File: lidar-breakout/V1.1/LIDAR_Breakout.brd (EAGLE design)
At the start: 36.5 x 88 mm, 89 parts, among them J1 UX60-MB-5S8, P1 MOLEX 0436500200, X1 TSX-3225 16.0000MF18X-AC0

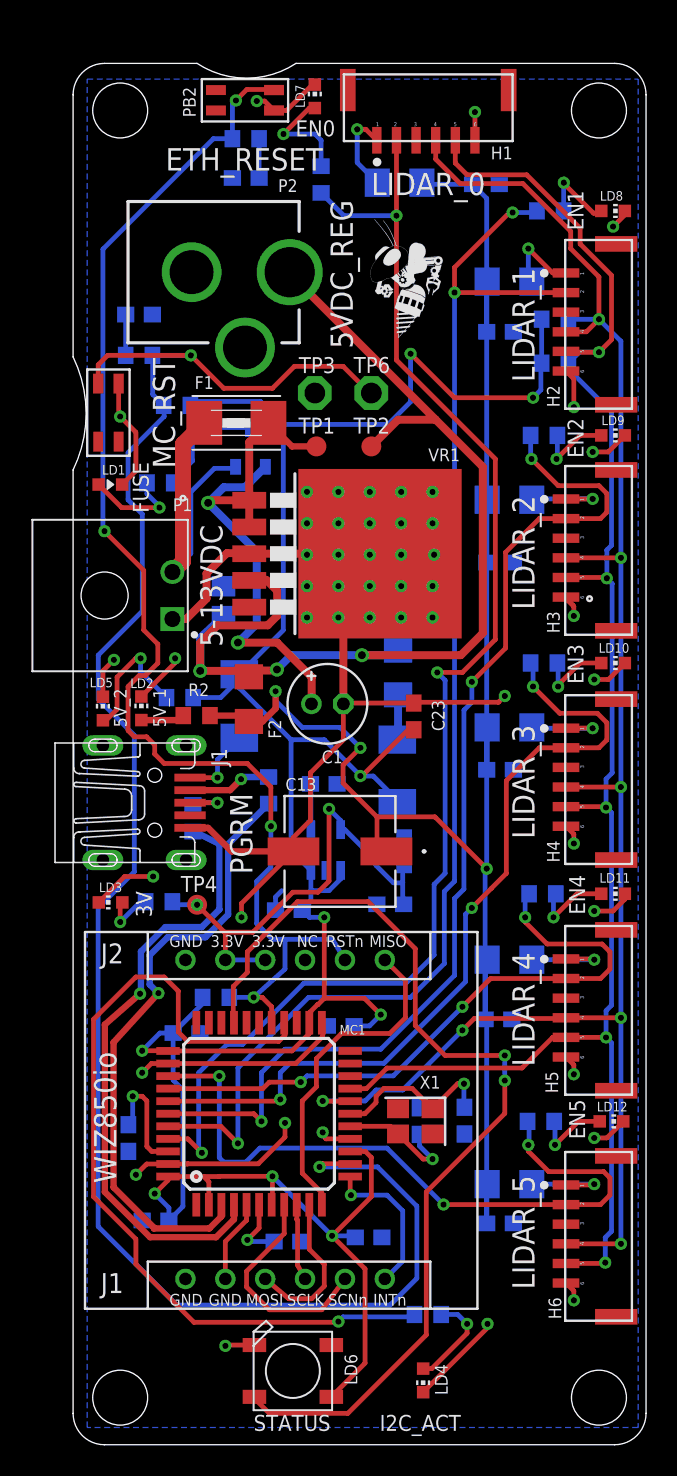
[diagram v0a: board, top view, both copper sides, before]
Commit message: Added POGO Pads
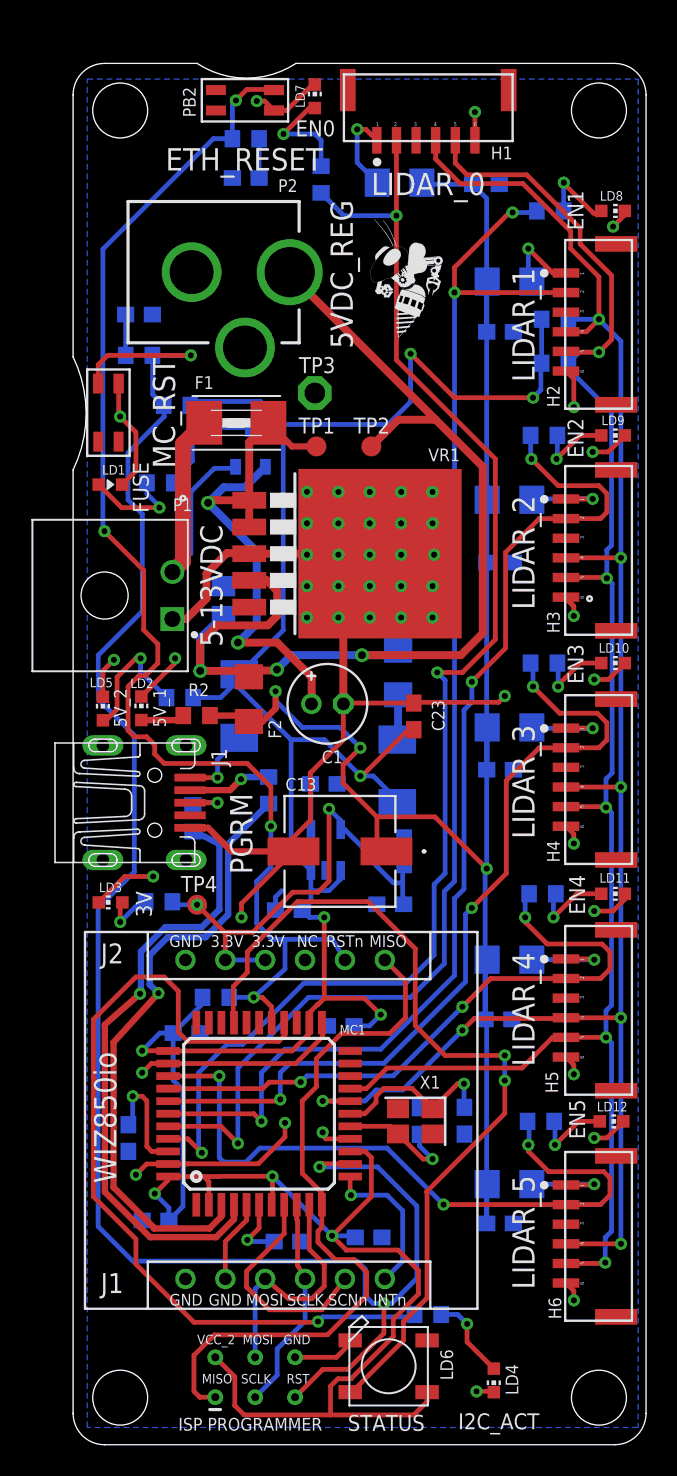
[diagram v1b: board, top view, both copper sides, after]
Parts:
- removed TP6: PTR1PAD1-13, testpad:P1-13
- added J2: AVR_SPI_PROG_3X2TESTPOINTS, SparkFun-Connectors:2X3_TEST_POINTS
- moved LD6 6.11 mm to (20.1, 5.00)
- moved LD4 4.50 mm to (26.8, 4.10)
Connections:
- net GND: now also J2.6
- net MISO_ETH: now also J2.1
- net MOSI_ETH: now also J2.4
- net RST_MC: now also J2.5; no longer TP6.TP
- net SCLK_ETH: now also J2.3
- net VCC_2: now also J2.2
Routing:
- net MISO_ETH: track 21.2 -> 45.4 mm
- net VCC_2: track 171.5 -> 194.9 mm
- net SCLK_ETH: track 4.86 -> 13.7 mm
- net STATUS_PWM: track 63.0 -> 55.2 mm
- net MOSI_ETH: track 10.1 -> 15.4 mm
- net RST_MC: track 120.6 -> 117.1 mm, vias 2 -> 3
- net GND: track 141.2 -> 138.4 mm, vias 49 -> 48
- net N$2: track 6.23 -> 5.45 mm
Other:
- board text added: "GND"
- board text added: "ISP PROGRAMMER"
- board text added: "MISO"
- board text added: "MOSI"
- board text added: "RST"
- board text added: "SCLK"
- board text added: "VCC_2"

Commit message: Updated Reset PB
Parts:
- PB1: device RoboJackets-Switches:RESET_PB_RA -> RoboJackets-Switches:TACT_PB_RA
- moved C26 10.9 mm to (15.1, 71.0)
- moved R19 6.24 mm to (10.3, 68.1), turned to 180 degrees
- moved P2 4.20 mm to (0.10, 78.9)
- moved PB1 4.20 mm to (0.00, 72.6)
- moved R7 3.00 mm to (15.8, 83.6)
- moved TP1 2.50 mm to (18.0, 63.6)
- moved H1 2.39 mm to (29.3, 89.3)
- moved C25 2.00 mm to (11.0, 82.7)
- moved LD7 2.00 mm to (15.4, 87.9)
- moved PB2 2.00 mm to (13.7, 89.0)
- moved R18 2.00 mm to (11.0, 85.2)
- moved TP2 2.00 mm to (21.0, 63.6)
- moved F1 1.92 mm to (12.3, 64.8)
- moved TP3 1.84 mm to (16.7, 68.3)
- moved R1 0.95 mm to (6.92, 67.1), turned to 90 degrees
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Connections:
- net GND: now also PB1.P$2; no longer PB1.P$3
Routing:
- net LDR0_EN: track 88.7 -> 93.7 mm
- net RST_MC: track 117.1 -> 112.7 mm, vias 3 -> 2
- net GND: track 138.4 -> 134.7 mm
- net RST_ETH: track 84.9 -> 88.3 mm
- net LDR0_LED: track 6.90 -> 4.20 mm
- net 5VREG: track 69.9 -> 72.2 mm
- net N$11: track 2.60 -> 4.30 mm
- net VCC_2: track 194.9 -> 193.5 mm
- net VIN: track 36.1 -> 37.1 mm
- net SCL: track 115.4 -> 114.5 mm
- net SDA: track 109.9 -> 109.1 mm
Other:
- board size 36.5 x 88 mm -> 36.5 x 90 mm

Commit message: Minor fixes/optimization
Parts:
- moved F1 1.40 mm to (13.7, 64.8)
- moved TP1 1.10 mm to (19.1, 63.6)
- moved TP2 1.10 mm to (22.1, 63.6)
- moved TP3 1.00 mm to (15.7, 68.3)
- moved P2 0.30 mm to (0.10, 78.6)
- moved R1 0.10 mm to (6.92, 67.2)
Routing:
- net GND: track 134.7 -> 145.7 mm
- net VIN: track 37.1 -> 36.0 mm
- net 5VREG: track 72.2 -> 71.2 mm
- net RST_MC: track 112.7 -> 113.4 mm

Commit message: Updated LED resistor values
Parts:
- R10, R11, R12, R7, R8, R9: value 1 kΩ -> 200Ω
- R13, R14, R17, R2, R3: value 1 kΩ -> 300Ω
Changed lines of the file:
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@@
 <attribute name="VALUE" x="10.547" y="41.055" size="1.27" layer="28" rot="MR90"/>
 </element>
-<element name="R14" library="rcl" library_urn="urn:adsk.eagle:library:334" package="R0603" package3d_urn="urn:adsk.eagle:package:23555/2" value="1 kΩ" x="5.558" y="61.277" smashed="yes" rot="MR0">
+<element name="R14" library="rcl" library_urn="urn:adsk.eagle:library:334" package="R0603" package3d_urn="urn:adsk.eagle:package:23555/2" value="300Ω" x="5.558" y="61.277" smashed="yes" rot="MR0">
 <attribute name="NAME" x="3.388" y="62.293" size="0.8128" layer="26" font="vector" rot="MR270"/>
 <attribute name="SPICEPREFIX" value="R" x="-32.542" y="-16.193" size="1.778" layer="28" rot="MR0" display="off"/>
 <attribute name="VALUE" x="6.193" y="59.372" size="1.27" layer="28" rot="MR0"/>
 </element>
-<element name="R2" library="rcl" library_urn="urn:adsk.eagle:library:334" package="R0603" package3d_urn="urn:adsk.eagle:package:23555/2" value="1 kΩ" x="7.869" y="46.45" smashed="yes">
+<element name="R2" library="rcl" library_urn="urn:adsk.eagle:library:334" package="R0603" package3d_urn="urn:adsk.eagle:package:23555/2" value="300Ω" x="7.869" y="46.45" smashed="yes">
 <attribute name="NAME" x="7.334" y="47.685" size="0.8128" layer="25" font="vector"/>
 <attribute name="SPICEPREFIX" value="R" x="37.079" y="-31.02" size="1.778" layer="27" display="off"/>
 <attribute name="VALUE" x="7.234" y="44.545" size="1.27" layer="27"/>
 </element>
-<element name="R13" library="rcl" library_urn="urn:adsk.eagle:library:334" package="R0603" package3d_urn="urn:adsk.eagle:package:23555/2" value="1 kΩ" x="5.472121875" y="34.5944" smashed="yes" rot="MR180">
+<element name="R13" library="rcl" library_urn="urn:adsk.eagle:library:334" package="R0603" package3d_urn="urn:adsk.eagle:package:23555/2" value="300Ω" x="5.472121875" y="34.5944" smashed="yes" rot="MR180">
 <attribute name="NAME" x="3.462878125" y="34.1406" size="0.8128" layer="26" font="vector" rot="MR0"/>
 <attribute name="SPICEPREFIX" value="R" x="61.352121875" y="112.0644" size="1.778" layer="28" rot="MR180" display="off"/>
@@
 <attribute name="NAME" x="7" y="88.5" size="0.8128" layer="21" font="vector" rot="R270"/>
 </element>
-<element name="R7" library="rcl" library_urn="urn:adsk.eagle:library:334" package="R0603" package3d_urn="urn:adsk.eagle:package:23555/2" value="1 kΩ" x="15.8" y="83.6" smashed="yes" rot="MR90">
+<element name="R7" library="rcl" library_urn="urn:adsk.eagle:library:334" package="R0603" package3d_urn="urn:adsk.eagle:package:23555/2" value="200Ω" x="15.8" y="83.6" smashed="yes" rot="MR90">
 <attribute name="NAME" x="16.435" y="80.935" size="0.8128" layer="26" font="vector" rot="MR0"/>
 <attribute name="SPICEPREFIX" value="R" x="15.8" y="83.6" size="1.778" layer="28" rot="MR90" display="off"/>
@@
 <attribute name="VALUE" x="17.305" y="87.265" size="1.27" layer="27" rot="R90"/>
 </element>
-<element name="R8" library="rcl" library_urn="urn:adsk.eagle:library:334" package="R0603" package3d_urn="urn:adsk.eagle:package:23555/2" value="1 kΩ" x="30.4" y="78.6" smashed="yes" rot="MR180">
+<element name="R8" library="rcl" library_urn="urn:adsk.eagle:library:334" package="R0603" package3d_urn="urn:adsk.eagle:package:23555/2" value="200Ω" x="30.4" y="78.6" smashed="yes" rot="MR180">
 <attribute name="NAME" x="29.765" y="77.365" size="0.8128" layer="26" font="vector" rot="MR180"/>
 <attribute name="SPICEPREFIX" value="R" x="30.4" y="78.6" size="1.778" layer="28" rot="MR180" display="off"/>
@@
 <attribute name="VALUE" x="33.765" y="76.695" size="1.27" layer="27"/>
 </element>
-<element name="R9" library="rcl" library_urn="urn:adsk.eagle:library:334" package="R0603" package3d_urn="urn:adsk.eagle:package:23555/2" value="1 kΩ" x="30" y="64.3" smashed="yes" rot="MR180">
+<element name="R9" library="rcl" library_urn="urn:adsk.eagle:library:334" package="R0603" package3d_urn="urn:adsk.eagle:package:23555/2" value="200Ω" x="30" y="64.3" smashed="yes" rot="MR180">
 <attribute name="NAME" x="27.335" y="63.765" size="0.8128" layer="26" font="vector" rot="MR90"/>
 <attribute name="SPICEPREFIX" value="R" x="30" y="64.3" size="1.778" layer="28" rot="MR180" display="off"/>
 <attribute name="VALUE" x="29.365" y="66.205" size="1.27" layer="28" rot="MR180"/>
 </element>
-<element name="R10" library="rcl" library_urn="urn:adsk.eagle:library:334" package="R0603" package3d_urn="urn:adsk.eagle:package:23555/2" value="1 kΩ" x="30" y="49.8" smashed="yes" rot="MR180">
+<element name="R10" library="rcl" library_urn="urn:adsk.eagle:library:334" package="R0603" package3d_urn="urn:adsk.eagle:package:23555/2" value="200Ω" x="30" y="49.8" smashed="yes" rot="MR180">
 <attribute name="NAME" x="29.065" y="51.765" size="0.8128" layer="26" font="vector" rot="MR180"/>
 <attribute name="SPICEPREFIX" value="R" x="30" y="49.8" size="1.778" layer="28" rot="MR180" display="off"/>
 <attribute name="VALUE" x="29.365" y="51.705" size="1.27" layer="28" rot="MR180"/>
 </element>
-<element name="R11" library="rcl" library_urn="urn:adsk.eagle:library:334" package="R0603" package3d_urn="urn:adsk.eagle:package:23555/2" value="1 kΩ" x="29.9" y="35.1" smashed="yes" rot="MR180">
+<element name="R11" library="rcl" library_urn="urn:adsk.eagle:library:334" package="R0603" package3d_urn="urn:adsk.eagle:package:23555/2" value="200Ω" x="29.9" y="35.1" smashed="yes" rot="MR180">
 <attribute name="NAME" x="31.935" y="34.165" size="0.8128" layer="26" font="vector" rot="SMR90"/>
 <attribute name="SPICEPREFIX" value="R" x="29.9" y="35.1" size="1.778" layer="28" rot="MR180" display="off"/>
 <attribute name="VALUE" x="29.265" y="37.005" size="1.27" layer="28" rot="MR180"/>
 </element>
-<element name="R12" library="rcl" library_urn="urn:adsk.eagle:library:334" package="R0603" package3d_urn="urn:adsk.eagle:package:23555/2" value="1 kΩ" x="29.8" y="20.6" smashed="yes" rot="MR180">
+<element name="R12" library="rcl" library_urn="urn:adsk.eagle:library:334" package="R0603" package3d_urn="urn:adsk.eagle:package:23555/2" value="200Ω" x="29.8" y="20.6" smashed="yes" rot="MR180">
 <attribute name="NAME" x="30.735" y="21.935" size="0.8128" layer="26" font="vector" rot="MR0"/>
 <attribute name="SPICEPREFIX" value="R" x="29.8" y="20.6" size="1.778" layer="28" rot="MR180" display="off"/>
@@
 <attribute name="VALUE" x="24.895" y="4.735" size="1.27" layer="27" rot="R270"/>
 </element>
-<element name="R3" library="rcl" library_urn="urn:adsk.eagle:library:334" package="R0603" package3d_urn="urn:adsk.eagle:package:23555/2" value="1 kΩ" x="22.6" y="8.3" smashed="yes" rot="MR0">
+<element name="R3" library="rcl" library_urn="urn:adsk.eagle:library:334" package="R0603" package3d_urn="urn:adsk.eagle:package:23555/2" value="300Ω" x="22.6" y="8.3" smashed="yes" rot="MR0">
 <attribute name="NAME" x="21.965" y="10.365" size="0.8128" layer="26" font="vector" rot="MR180"/>
 <attribute name="SPICEPREFIX" value="R" x="22.6" y="8.3" size="1.778" layer="28" rot="MR0" display="off"/>
@@
 <attribute name="VALUE" x="23.113" y="50.597" size="1.27" layer="28" rot="MR270"/>
 </element>
-<element name="R17" library="rcl" library_urn="urn:adsk.eagle:library:334" package="R0603" package3d_urn="urn:adsk.eagle:package:23555/2" value="1 kΩ" x="6.8" y="47.6" smashed="yes" rot="MR180">
+<element name="R17" library="rcl" library_urn="urn:adsk.eagle:library:334" package="R0603" package3d_urn="urn:adsk.eagle:package:23555/2" value="300Ω" x="6.8" y="47.6" smashed="yes" rot="MR180">
 <attribute name="NAME" x="4.035" y="46.665" size="0.8128" layer="26" rot="MR90"/>
 <attribute name="SPICEPREFIX" value="R" x="6.8" y="47.6" size="1.778" layer="28" rot="MR180" display="off"/>

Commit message: Minor Changes, DRC, Design Review Prep
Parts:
- moved TP3 0.50 mm to (15.7, 68.8)
- moved C26 0.40 mm to (15.1, 71.4)
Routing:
- net GND: track 145.7 -> 156.7 mm, vias 48 -> 44
- net RST_MC: track 113.4 -> 114.7 mm
- net VCC_2: track 193.6 -> 194.4 mm
- net RST_ETH: track 88.3 -> 87.5 mm

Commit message: DR Ready
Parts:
- moved C11 0.70 mm to (27.2, 70.2)
- moved C21 0.58 mm to (20.8, 37.3)
- moved C6 0.50 mm to (20.2, 33.9)
- moved R5 0.20 mm to (30.9, 68.9)
- moved R6 0.20 mm to (30.9, 71.7)
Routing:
- net VCC_1: track 119.5 -> 120.2 mm

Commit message: Design Review Updates
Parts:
- C25: value 1 uF -> 0.1uF
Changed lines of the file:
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@@
 <?xml version="1.0" encoding="utf-8"?>
 <!DOCTYPE eagle SYSTEM "eagle.dtd">
-<eagle version="9.3.0">
+<eagle version="9.2.2">
 <drawing>
 <settings>
-<setting alwaysvectorfont="yes"/>
+<setting alwaysvectorfont="no"/>
 <setting verticaltext="up"/>
 </settings>
 <grid distance="0.1" unitdist="mm" unit="mm" style="lines" multiple="1" display="yes" altdistance="0.05" altunitdist="mm" altunit="mm"/>
 <layers>
-<layer number="1" name="Top" color="4" fill="1" visible="yes" active="yes"/>
+<layer number="1" name="Top" color="4" fill="1" visible="no" active="yes"/>
 <layer number="2" name="Route2" color="16" fill="1" visible="no" active="no"/>
 <layer number="3" name="Route3" color="17" fill="1" visible="no" active="no"/>
@@
 <layer number="19" name="Unrouted" color="6" fill="1" visible="yes" active="yes"/>
 <layer number="20" name="Dimension" color="24" fill="1" visible="yes" active="yes"/>
-<layer number="21" name="tPlace" color="7" fill="1" visible="yes" active="yes"/>
+<layer number="21" name="tPlace" color="7" fill="1" visible="no" active="yes"/>
 <layer number="22" name="bPlace" color="7" fill="1" visible="yes" active="yes"/>
-<layer number="23" name="tOrigins" color="15" fill="1" visible="yes" active="yes"/>
+<layer number="23" name="tOrigins" color="15" fill="1" visible="no" active="yes"/>
 <layer number="24" name="bOrigins" color="15" fill="1" visible="yes" active="yes"/>
-<layer number="25" name="tNames" color="7" fill="1" visible="yes" active="yes"/>
+<layer number="25" name="tNames" color="7" fill="1" visible="no" active="yes"/>
 <layer number="26" name="bNames" color="7" fill="1" visible="yes" active="yes"/>
 <layer number="27" name="tValues" color="7" fill="1" visible="no" active="yes"/>
@@
 <layer number="37" name="tTest" color="7" fill="1" visible="no" active="yes"/>
 <layer number="38" name="bTest" color="7" fill="1" visible="no" active="yes"/>
-<layer number="39" name="tKeepout" color="4" fill="11" visible="yes" active="yes"/>
+<layer number="39" name="tKeepout" color="4" fill="11" visible="no" active="yes"/>
 <layer number="40" name="bKeepout" color="1" fill="11" visible="yes" active="yes"/>
-<layer number="41" name="tRestrict" color="4" fill="10" visible="yes" active="yes"/>
+<layer number="41" name="tRestrict" color="4" fill="10" visible="no" active="yes"/>
 <layer number="42" name="bRestrict" color="1" fill="10" visible="yes" active="yes"/>
 <layer number="43" name="vRestrict" color="2" fill="10" visible="no" active="yes"/>
@@
 <layer number="49" name="Reference" color="7" fill="1" visible="no" active="yes"/>
 <layer number="50" name="dxf" color="7" fill="1" visible="no" active="no"/>
-<layer number="51" name="tDocu" color="7" fill="1" visible="yes" active="yes"/>
+<layer number="51" name="tDocu" color="7" fill="1" visible="no" active="yes"/>
 <layer number="52" name="bDocu" color="7" fill="1" visible="yes" active="yes"/>
 <layer number="53" name="tGND_GNDA" color="7" fill="9" visible="no" active="no"/>
@@
 <text x="8.1" y="58.6" size="1.4224" layer="21" font="vector" rot="R270">5-13VDC</text>
 <text x="10" y="41.5" size="1.4224" layer="21" font="vector" rot="R270">PGRM</text>
-<wire x1="14.2" y1="90" x2="7.9" y2="90" width="0.0762" layer="20" curve="-66.549776"/>
+<wire x1="14.2" y1="90" x2="7.9" y2="90" width="0" layer="20" curve="-66.549776"/>
 <wire x1="29.3" y1="72.7" x2="32.5" y2="72.7" width="0.1016" layer="22"/>
 <wire x1="32.5" y1="72.7" x2="32.5" y2="70.7" width="0.1016" layer="22"/>
@@
 <attribute name="PINS" value="5" x="-1.2" y="40.9" size="1.778" layer="27" display="off"/>
 </element>
-<element name="C25" library="resistor" library_urn="urn:adsk.eagle:library:348" package="C0603" package3d_urn="urn:adsk.eagle:package:26138/1" value="1 uF" x="11" y="82.7" smashed="yes" rot="MR0">
+<element name="C25" library="resistor" library_urn="urn:adsk.eagle:library:348" package="C0603" package3d_urn="urn:adsk.eagle:package:26138/1" value="0.1uF" x="11" y="82.7" smashed="yes" rot="MR0">
 <attribute name="NAME" x="8.135" y="81.765" size="0.8128" layer="26" rot="MR90"/>
 <attribute name="VALUE" x="11.635" y="80.795" size="1.27" layer="28" rot="MR0"/>

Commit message: Post Design Review Updates
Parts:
- removed R18, R19: 1 kΩ, rcl:R0603
- D1, D2: value (none) -> APD340VRTR-G1
- R13, R14, R17, R2, R3: value 300Ω -> 330Ω
- moved C26 5.42 mm to (10.8, 68.1)
- moved R3 2.73 mm to (25.0, 9.60)
- moved C25 2.50 mm to (11.0, 85.2), turned to 180 degrees
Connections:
- removed net N$10: C25.1, R18.2
- removed net N$11: C26.1, R19.2
- net RST_ETH: now also C25.1; no longer R18.1
- net RST_MC: now also C26.1; no longer R19.1
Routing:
- net N$11: track 4.58 -> 0.00 mm
- net I2C_ACT: track 53.7 -> 56.7 mm
- net GND: track 156.6 -> 159.4 mm
- net N$10: track 2.50 -> 0.00 mm
- net RST_MC: track 114.7 -> 113.6 mm
- net N$2: track 5.45 -> 6.27 mm
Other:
- board text added: "LIDAR BREAKOUT REV: 1.1 (2019)"
- board text removed: "LIDAR BREAKOUT VERSION: 1.1 2019"
